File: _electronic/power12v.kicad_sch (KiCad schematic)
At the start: 3 parts

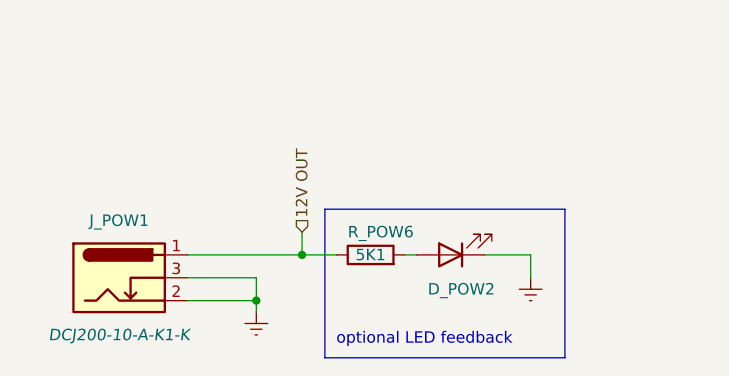
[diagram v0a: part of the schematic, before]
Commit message: BETA first upload
nothing major done here:
* updated KiCAD files to v9
* removed alternative 6v feed-in. The proposed buck converter is fine.
* added to all components LCSC component IDs. With this, exporting the project as gerber files also automatically creates correct BOM for JLCPCB manufacturing
*
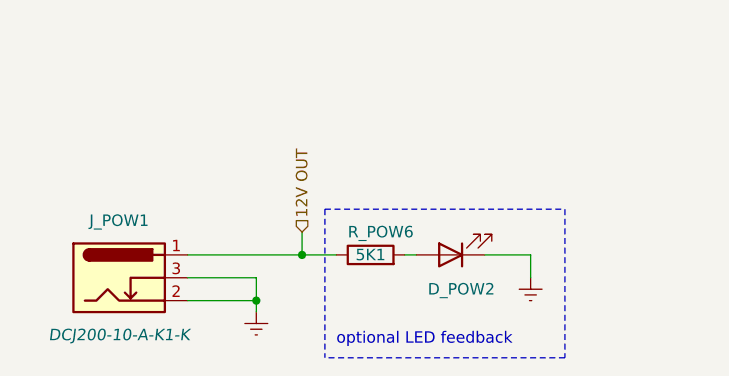
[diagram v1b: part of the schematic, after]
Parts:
- D_POW2: LCSC (none) -> C2290
- R_POW6: LCSC (none) -> C23186
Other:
- title: E-TKT v1.0 -> E-TKT v2.0 BETA

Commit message: Added CAD, cleaned up KiCAD some more
Added a FreeCAD Assembly. This will serve for minor updated to the printable parts.
Updated USB-C component to standard KiCAD libary-integrated version, because the pinout of the schematic symbol was messing with the pinout of the footprint
exported the PCB as step so it could be imported to FreeCAD
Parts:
- J_POW1: footprint SnapEDA Library:BarrelJack_GCT_DCJ200-10-A_Horizontal -> EASYEDA2KICAD:BarrelJack_Horizontal
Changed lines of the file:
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@@
 			)
 		)
-		(property "Footprint" "SnapEDA Library:BarrelJack_GCT_DCJ200-10-A_Horizontal"
+		(property "Footprint" "EASYEDA2KICAD:BarrelJack_Horizontal"
 			(at 123.19 89.916 0)
 			(effects

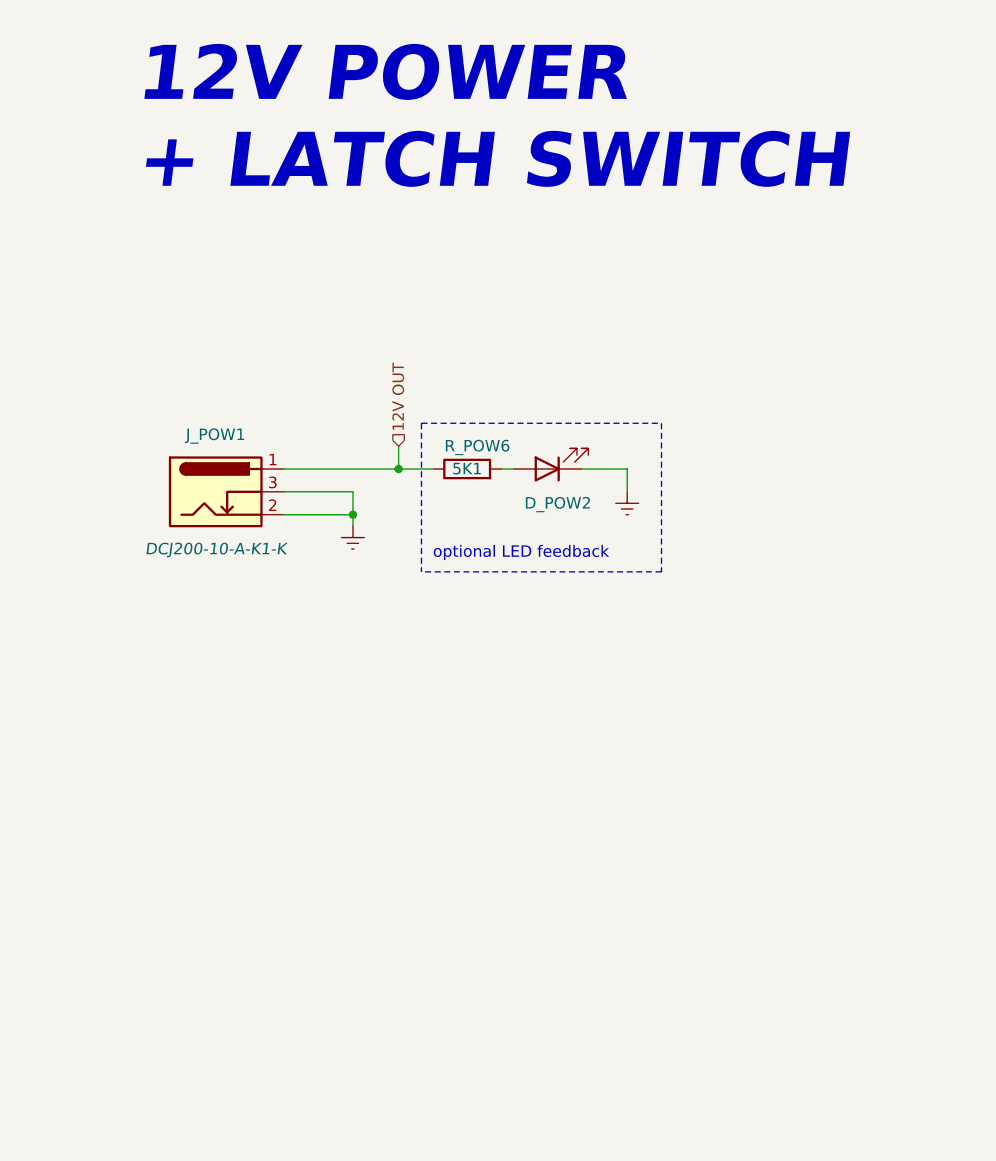
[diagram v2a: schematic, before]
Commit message: USB-C PD added
in parallel to DC jack, realized via HUSB237
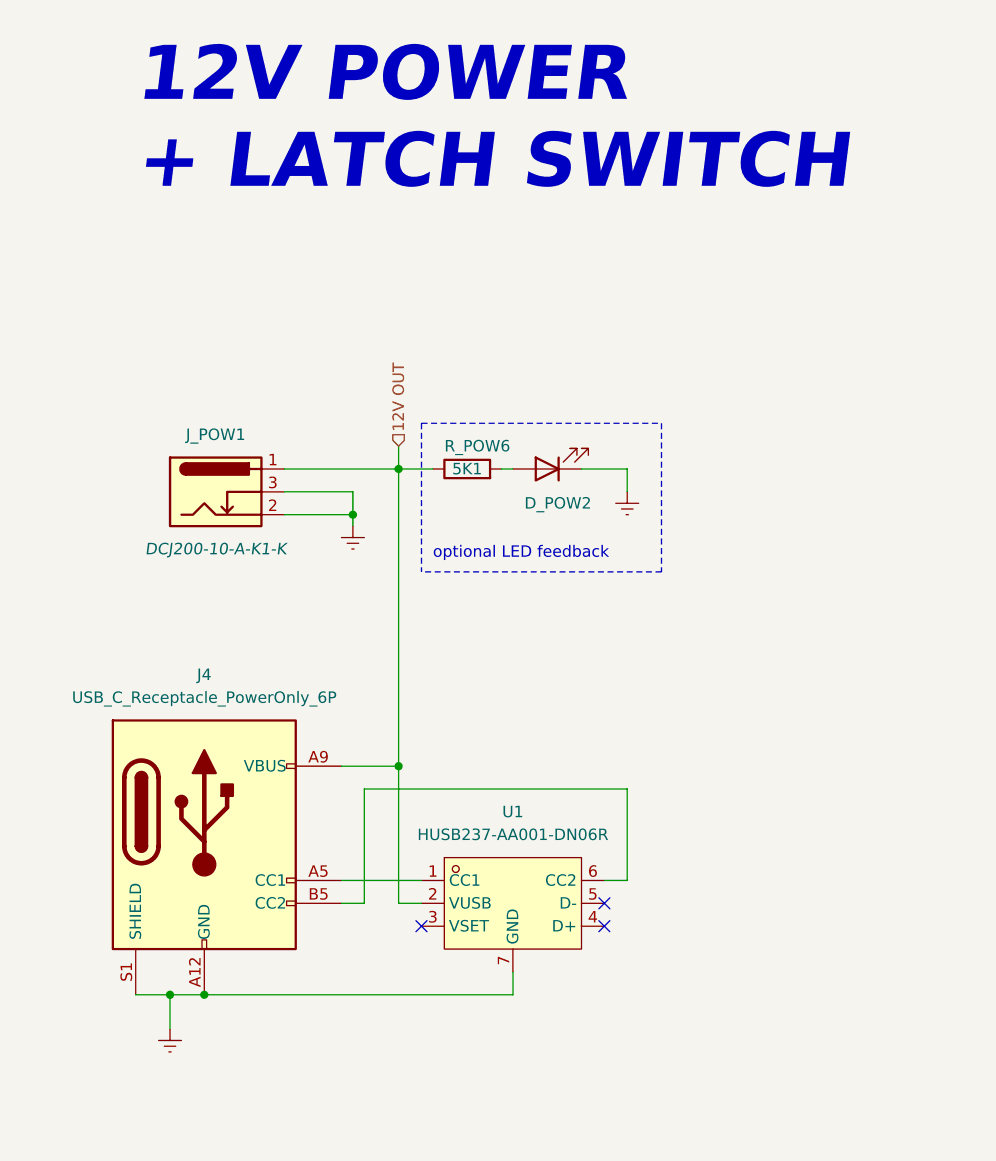
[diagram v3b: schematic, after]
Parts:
- added J4: USB_C_Receptacle_PowerOnly_6P, EASYEDA2KICAD:USB-C-TH_TYPE-C-6PLCH10.0-073, symbol Connector:USB_C_Receptacle_PowerOnly_6P
- added U1: HUSB237-AA001-DN06R, EASYEDA2KICAD:TDFN-6_L2.0-W2.0-P0.65-TL-EP, symbol EASYEDA2KICAD:HUSB237-AA001-DN06R
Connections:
- net 12V OUT: now also J4.A9 (VBUS), J4.B9 (VBUS), U1.2 (VUSB)
- net GNDREF: now also J4.A12 (GND), J4.B12 (GND), J4.S1 (SHIELD), U1.7 (GND)
- new net: J4.A5 (CC1), U1.1 (CC1)
- new net: J4.B5 (CC2), U1.6 (CC2)
- no-connect marks 0 -> 3

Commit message: Optimized alignment of USB-C socket
so that there is more tolerance for printed parts
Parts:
- J4: footprint EASYEDA2KICAD:USB-C-TH_TYPE-C-6PLCH10.0-073 -> EASYEDA2KICAD:USB-C-TH_TYPE-604-T3-5A; LCSC C5156601 -> C7464651
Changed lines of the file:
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@@
 			)
 		)
-		(property "Footprint" "EASYEDA2KICAD:USB-C-TH_TYPE-C-6PLCH10.0-073"
+		(property "Footprint" "EASYEDA2KICAD:USB-C-TH_TYPE-604-T3-5A"
 			(at 124.46 124.46 0)
 			(effects
@@
 			)
 		)
-		(property "LCSC" "C5156601"
+		(property "LCSC" "C7464651"
 			(at 120.65 127 0)
 			(effects

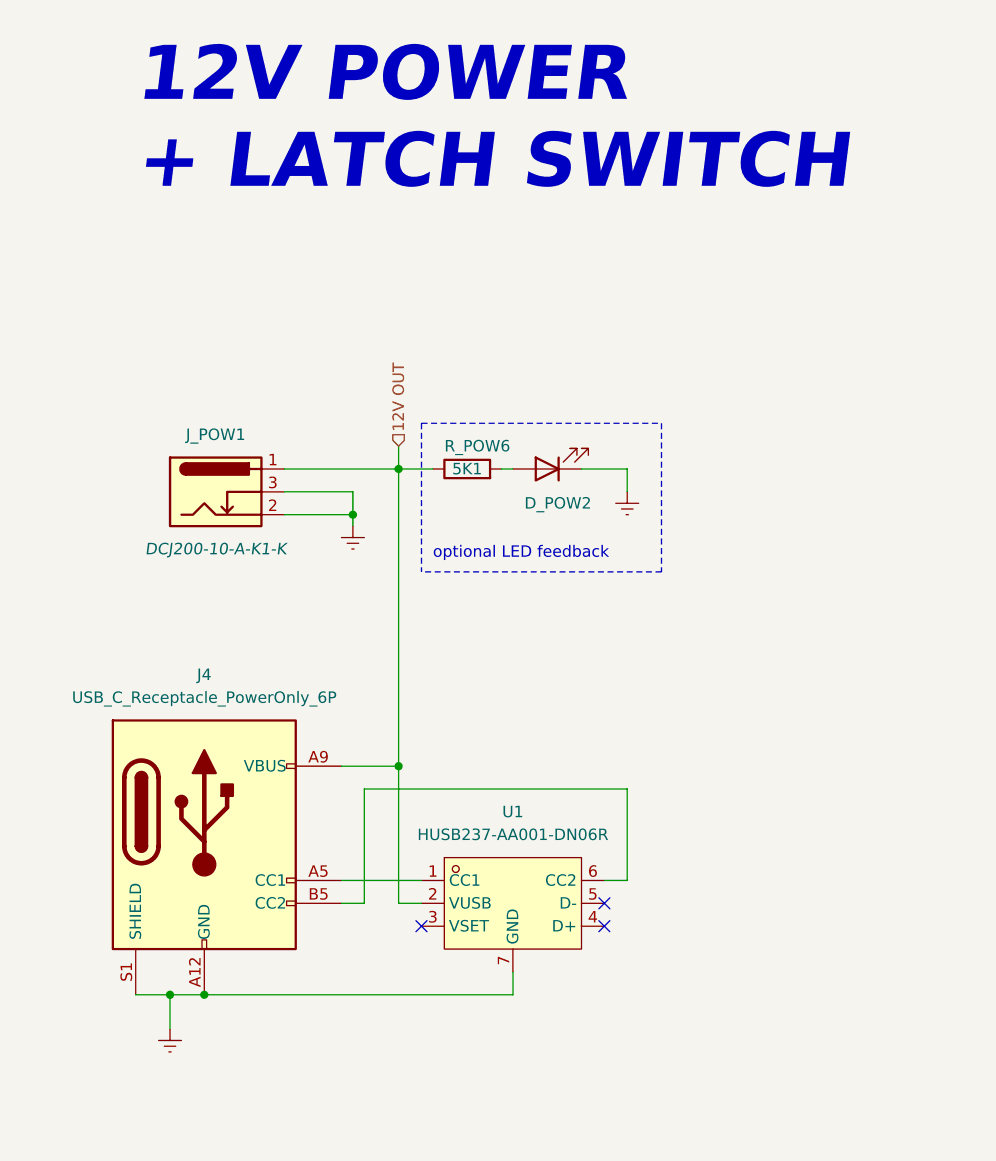
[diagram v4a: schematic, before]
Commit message: Added endstop
added footprint for a microswitch with roller as enstop. updated the CAD correspondingly by adding M4 hole in the nema wheel hub for an M4 12mm/16mm set screw (the ones with a pointy end).
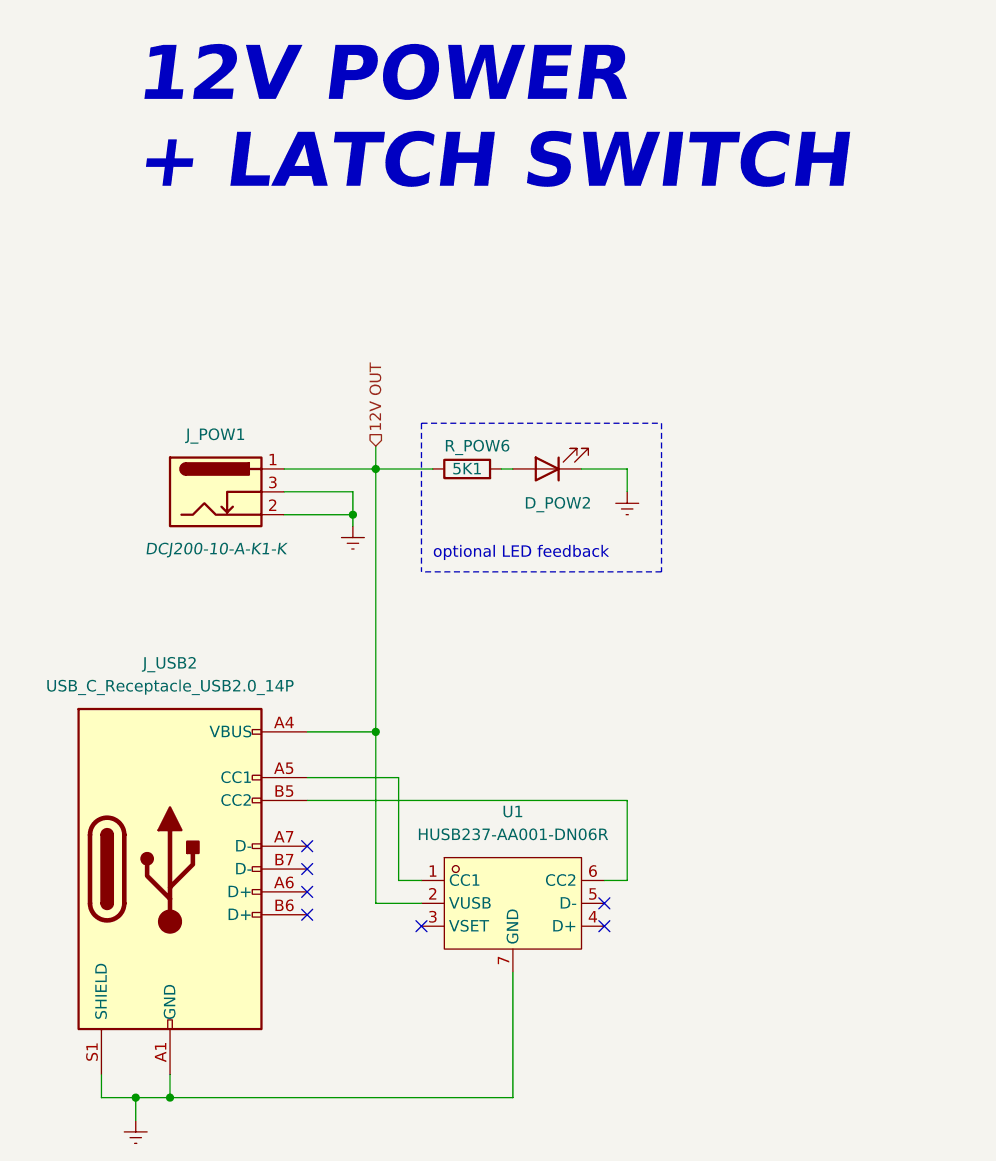
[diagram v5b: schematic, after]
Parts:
- removed J4: USB_C_Receptacle_PowerOnly_6P, EASYEDA2KICAD:USB-C-TH_TYPE-604-T3-5A, symbol Connector:USB_C_Receptacle_PowerOnly_6P
- added J_USB2: USB_C_Receptacle_USB2.0_14P, EASYEDA2KICAD:USB-TH_GT-USB-7057A, symbol Connector:USB_C_Receptacle_USB2.0_14P
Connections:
- net 12V OUT: now also J_USB2.A4 (VBUS), J_USB2.A9 (VBUS), J_USB2.B4 (VBUS), J_USB2.B9 (VBUS)
- net GNDREF: now also J_USB2.A1 (GND), J_USB2.A12 (GND), J_USB2.B1 (GND), J_USB2.B12 (GND), J_USB2.S1 (SHIELD)
- net at U1.1 (CC1): now also J_USB2.A5 (CC1)
- net at U1.6 (CC2): now also J_USB2.B5 (CC2)
- no-connect marks 3 -> 7

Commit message: sturdyfy E-TKT
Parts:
- J_USB2: symbol Connector:USB_C_Receptacle_USB2.0_14P -> EASYEDA2KICAD:USB_C_Receptacle_USB2.0_8P
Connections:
- net 12V OUT: no longer J_USB2.A9 (VBUS), J_USB2.B4 (VBUS), J_USB2.B9 (VBUS)
- net GNDREF: no longer J_USB2.A12 (GND), J_USB2.B1 (GND), J_USB2.B12 (GND)
- no-connect marks 7 -> 5
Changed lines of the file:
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@@
-	)
-	(no_connect
-		(at 132.08 130.81)
-	)
-	(no_connect
-		(at 132.08 135.89)
 	)
 	(no_connect
@@
 	)
 	(symbol
-		(lib_id "Connector:USB_C_Receptacle_USB2.0_14P")
+		(lib_id "EASYEDA2KICAD:USB_C_Receptacle_USB2.0_8P")
 		(at 116.84 130.81 0)
 		(unit 1)
@@
 			)
 		)
-		(pin "A9"
-		)
-		(pin "A12"
-		)
 		(pin "A1"
 		)
 		(pin "S1"
 		)
-		(pin "B1"
-		)
-		(pin "B12"
-		)
 		(pin "A4"
 		)
-		(pin "B4"
-		)
-		(pin "B9"
-		)
 		(pin "A5"
 		)
@@
 		(pin "A6"
 		)
-		(pin "B6"
-		)
-		(pin "B7"
-		)
 		(pin "A7"

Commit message: JLC export added, LCSC numbers updated
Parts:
- J_USB2: LCSC (none) -> C22383830
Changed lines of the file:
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@@
+			)
+		)
+		(property "LCSC" "C22383830"
+			(at 116.84 130.81 0)
+			(effects
+				(font
+					(size 1.27 1.27)
+				)
+				(hide yes)
 			)
 		)

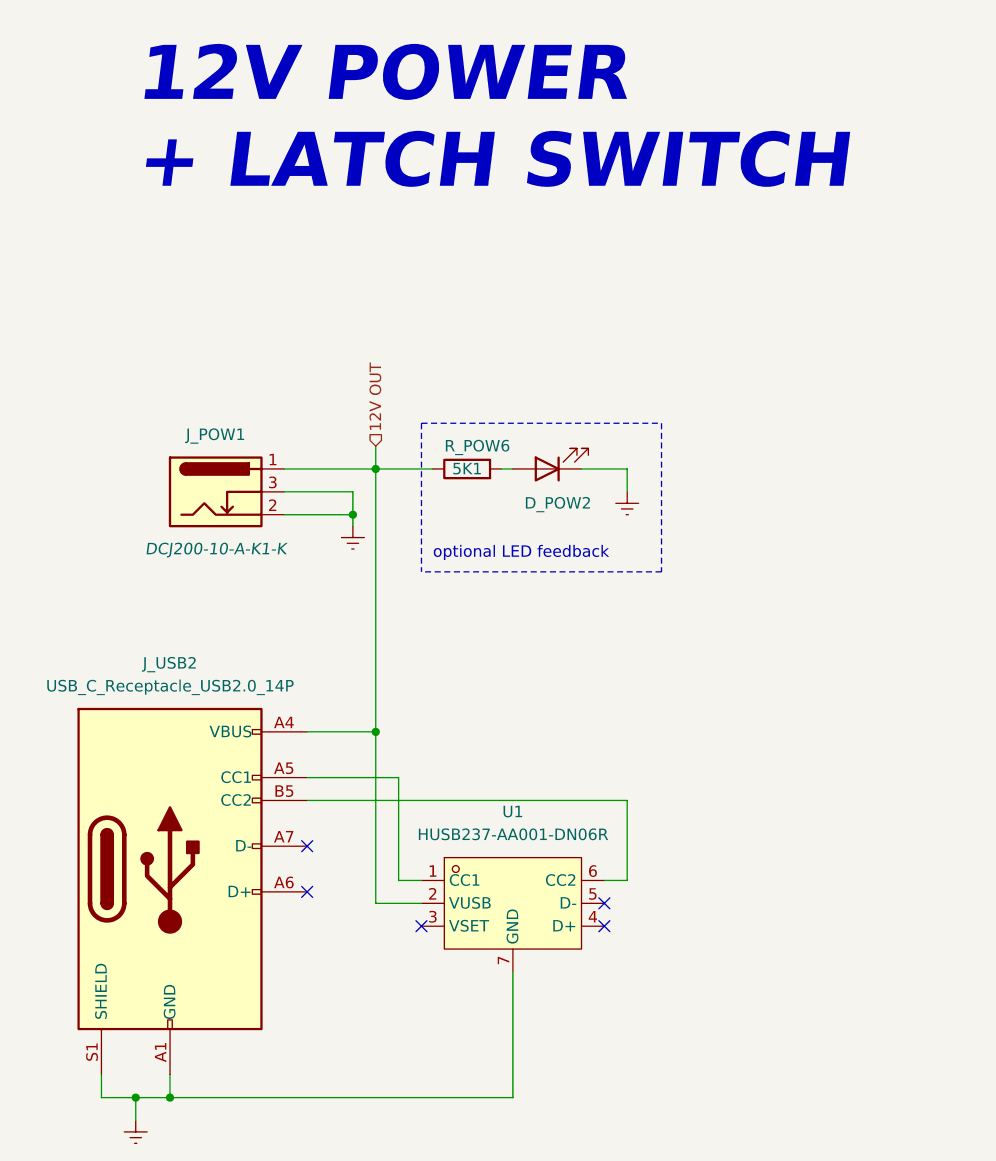
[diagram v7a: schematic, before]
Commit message: Updated layout of schematic symbol's text
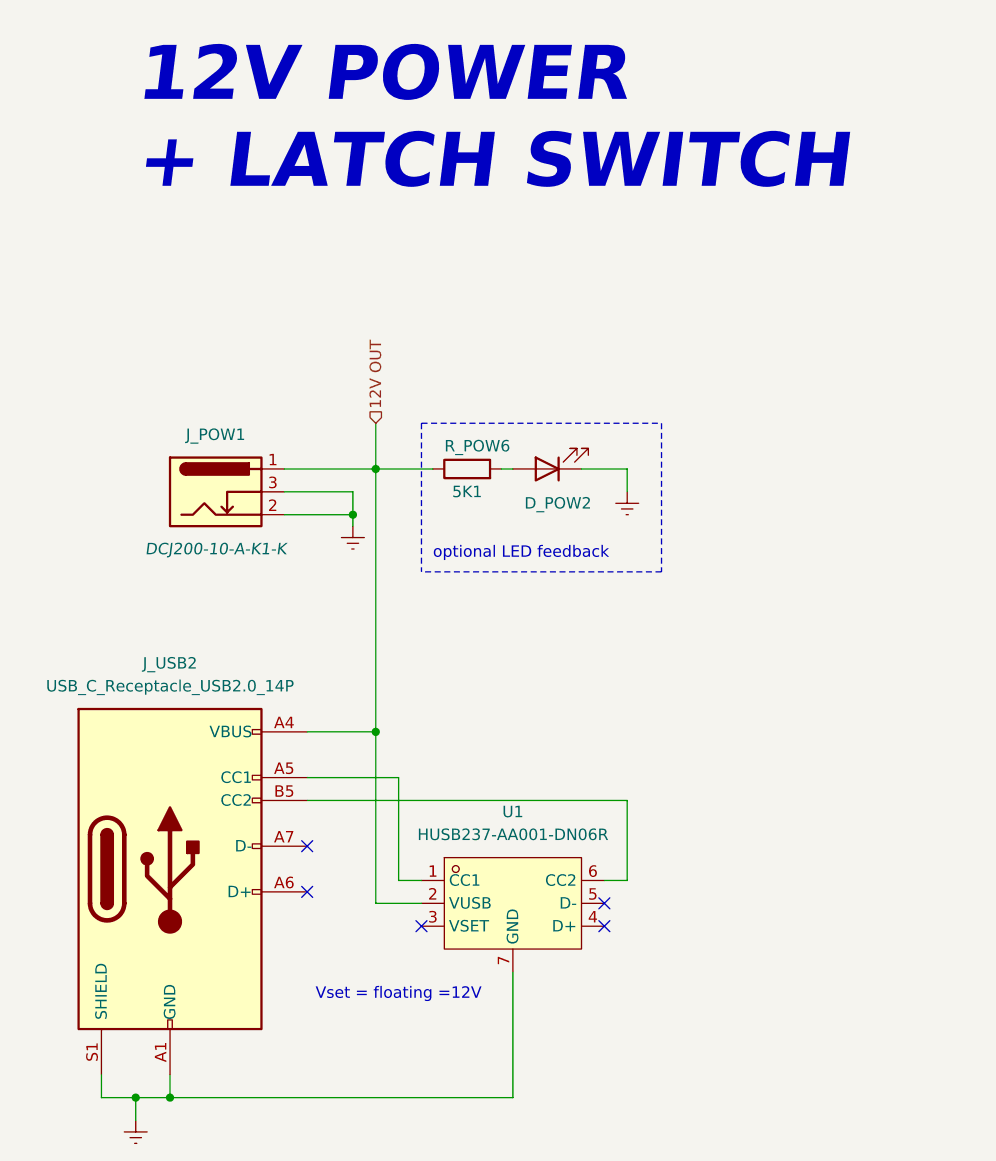
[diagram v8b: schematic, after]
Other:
- note added: "Vset = floating =12V"
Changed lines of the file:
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@@
 		(company "Andrei Speridiao")
+	)
+	(text "Vset = floating =12V"
+		(exclude_from_sim no)
+		(at 142.24 144.78 0)
+		(effects
+			(font
+				(size 1.27 1.27)
+			)
+		)
 	)
 	(text "optional LED feedback"
@@
 	(wire
 		(pts
-			(xy 139.7 83.82) (xy 139.7 86.36)
+			(xy 139.7 81.28) (xy 139.7 86.36)
 		)
 		(stroke
@@
 	(hierarchical_label "12V OUT"
 		(shape input)
-		(at 139.7 83.82 90)
+		(at 139.7 81.28 90)
 		(effects
 			(font
@@
 		)
 		(property "Value" "5K1"
-			(at 149.86 86.36 90)
-			(effects
-				(font
+			(at 149.86 88.9 90)
+			(effects
+				(font
